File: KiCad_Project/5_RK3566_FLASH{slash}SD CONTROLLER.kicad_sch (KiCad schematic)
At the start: 8 parts

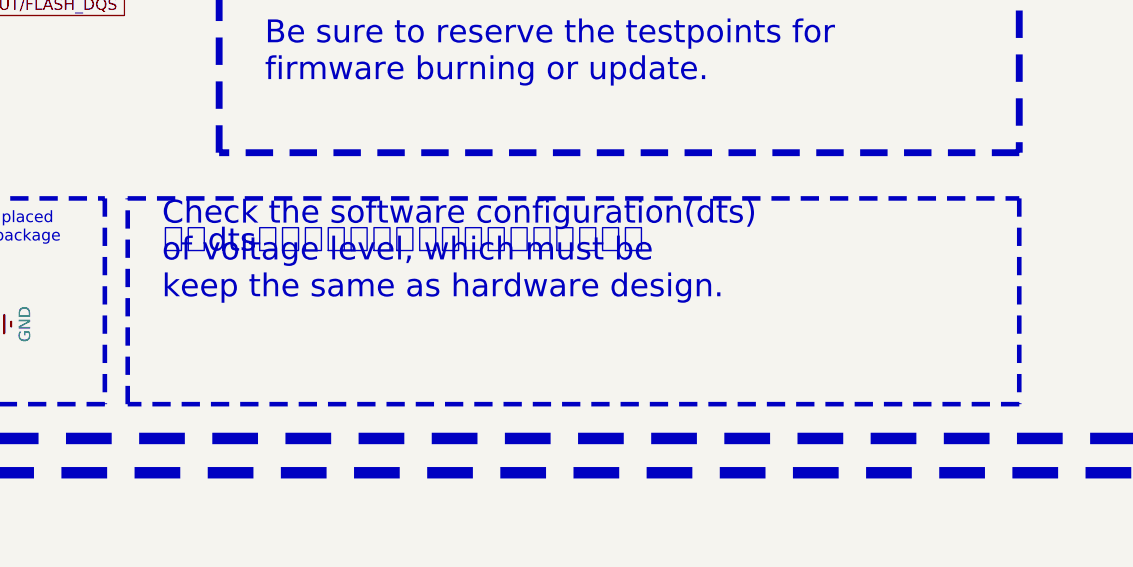
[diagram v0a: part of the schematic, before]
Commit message: Update additional PCBs
Add WIFI PCB to get best antenna
Add Display Debbugger to get interface pinout
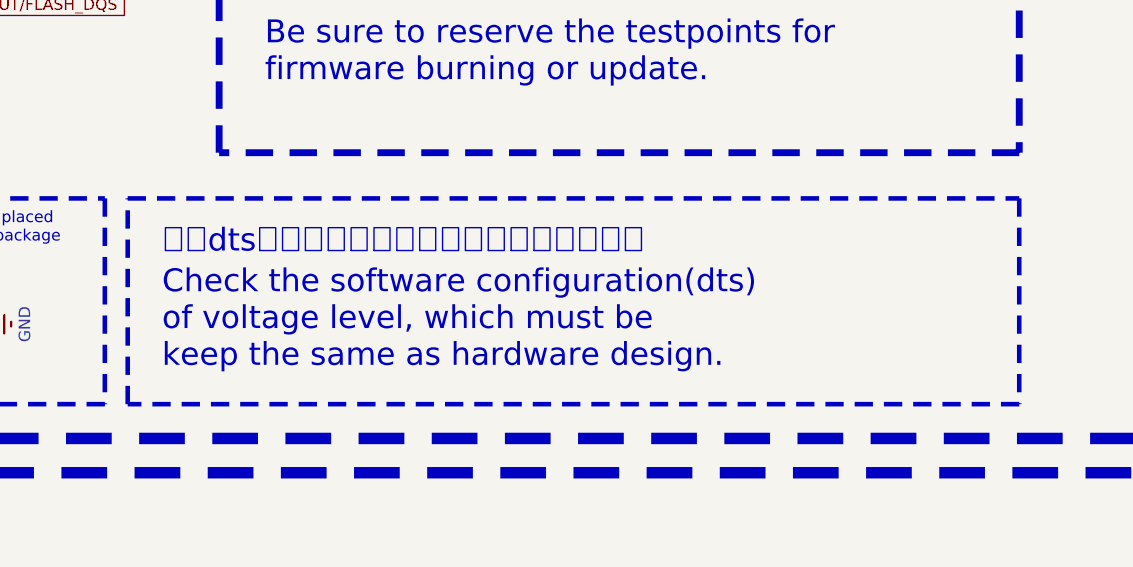
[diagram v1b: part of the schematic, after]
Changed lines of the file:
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@@
 	(text "Check the software configuration(dts)\nof voltage level, which must be\nkeep the same as hardware design."
 		(exclude_from_sim no)
-		(at 220.98 114.3 0)
+		(at 220.98 121.92 0)
 		(effects
 			(font
